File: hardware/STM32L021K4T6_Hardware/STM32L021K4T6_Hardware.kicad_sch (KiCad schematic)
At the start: 1 part, among them U1 STM32L021K4Tx

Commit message: schematic and footprints
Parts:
- added C1: 4u7, Capacitor_SMD:C_0805_2012Metric_Pad1.18x1.45mm_HandSolder, symbol Device:C_Small
- added C10: 10u, Capacitor_SMD:C_0805_2012Metric, symbol Device:C_Small
- added C2, C3, C6, C9: 100n, Capacitor_SMD:C_0805_2012Metric_Pad1.18x1.45mm_HandSolder, symbol Device:C_Small
- added C4: 1u, Capacitor_SMD:C_0805_2012Metric_Pad1.18x1.45mm_HandSolder, symbol Device:C_Small
- added C5: 10n, Capacitor_SMD:C_0805_2012Metric_Pad1.18x1.45mm_HandSolder, symbol Device:C_Small
- added C7, C8: 1uF, Capacitor_SMD:C_0805_2012Metric, symbol Device:C_Small
- added D1, D2: ~, LED_SMD:LED_0603_1608Metric_Pad1.05x0.95mm_HandSolder, symbol Device:LED_Small
- added J1: Conn_02x07_Odd_Even, Connector_PinHeader_1.27mm:PinHeader_2x07_P1.27mm_Vertical_SMD, symbol Connector_Generic:Conn_02x07_Odd_Even
- added J2: INPUT, Connector_JST:JST_XH_B2B-XH-A_1x02_P2.50mm_Vertical, symbol Connector_Generic:Conn_01x02
- added J3: POWER, Connector_JST:JST_XH_B2B-XH-A_1x02_P2.50mm_Vertical, symbol Connector_Generic:Conn_01x02
- added J4: OUTPUT, Connector_JST:JST_XH_B2B-XH-A_1x02_P2.50mm_Vertical, symbol Connector_Generic:Conn_01x02
- added L1: 39n, Inductor_SMD:L_0805_2012Metric_Pad1.05x1.20mm_HandSolder, symbol Device:L_Small
- added R1, R3: 1k, Resistor_SMD:R_0805_2012Metric_Pad1.20x1.40mm_HandSolder, symbol Device:R_Small
- added R2: 100k, Resistor_SMD:R_0805_2012Metric_Pad1.20x1.40mm_HandSolder, symbol Device:R_Small
- added U2: MCP1802x-xx02xOT, Package_TO_SOT_SMD:SOT-23-5, symbol Regulator_Linear:MCP1802x-xx02xOT
- added U3: MCP4801, Package_SO:SOIC-8_3.9x4.9mm_P1.27mm, symbol Analog_DAC:MCP4801
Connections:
- net +3.3V: now also C1.1, C2.1, C3.1, C8.1, D2.2 (A), J1.3 (Pin_3), L1.1, U2.5 (VOUT)
- net +3.3VA: now also C10.1, C4.1, C5.1, C9.1, L1.2, U3.1 (Vdd), U3.6 (~{SHDN})
- net GND: now also C1.2, C10.2, C2.2, C3.2, C4.2, C5.2, C6.2, C7.2, C8.2, C9.2, J1.11 (Pin_11), J1.5 (Pin_5), J1.7 (Pin_7), J2.2 (Pin_2), J3.2 (Pin_2), J4.2 (Pin_2), R1.2, R2.2, R3.2, U2.2 (GND), U3.7 (Vss)
- net DAC_nCS: now reaches U1.10 (PA4)
- net DAC_nCS: now also U3.2 (~{CS})
- net SPI1_SCK: now reaches U1.11 (PA5)
- net SPI1_SCK: now also U3.3 (SCK)
- net SPI1_MOSI: now reaches U1.13 (PA7)
- net SPI1_MOSI: now also U3.4 (SDI)
- net LED_STATUS: now reaches U1.18 (PA8)
- net LED_STATUS: now also D1.2 (A)
- net SWDIO: now reaches U1.23 (PA13)
- net SWDIO: now also J1.4 (Pin_4)
- net SWDCK: now reaches U1.24 (PA14)
- net SWDCK: now also J1.6 (Pin_6)
- net at U1.31 (PB9): now also R2.1
- net NRST: now reaches U1.4 (NRST)
- net NRST: now also C6.1, J1.12 (Pin_12)
- net USART2_RX: now reaches U1.6 (PA0)
- net USART2_RX: now also J1.13 (Pin_13)
- net ADC_IN1: now reaches U1.7 (PA1)
- net ADC_IN1: now also J2.1 (Pin_1)
- net USART2_TX: now reaches U1.8 (PA2)
- net USART2_TX: now also J1.14 (Pin_14)
- net DAC_nLDAC: now reaches U1.9 (PA3)
- net DAC_nLDAC: now also U3.5 (~{LDAC})
- new net: D1.1 (K), R1.1
- new net: D2.1 (K), R3.1
- new net +5V: C7.1, J3.1 (Pin_1), U2.1 (VIN), U2.3 (~{SHDN})
- new net DAC_OUT: J4.1 (Pin_1), U3.8 (Vout)
- no-connect marks 0 -> 20
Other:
- note added: "DAC MCP4801"
- note added: "IO Connectors"
- note added: "Power supply"
- note added: "STM32 Microcontroller"
- note added: "SWD Connector"

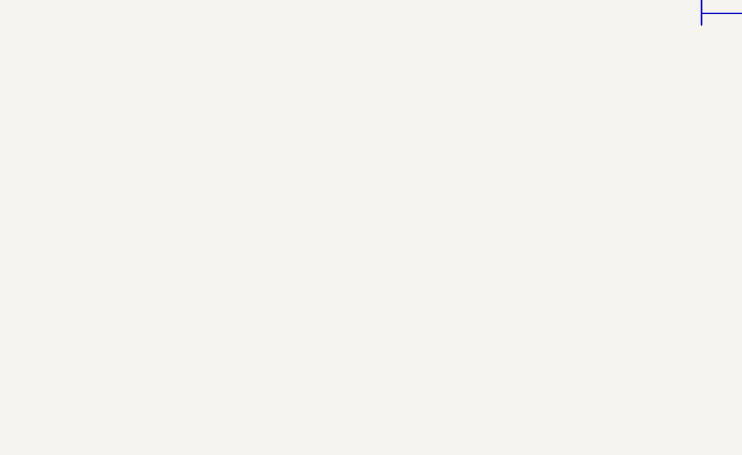
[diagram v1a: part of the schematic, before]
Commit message: add mounting holes
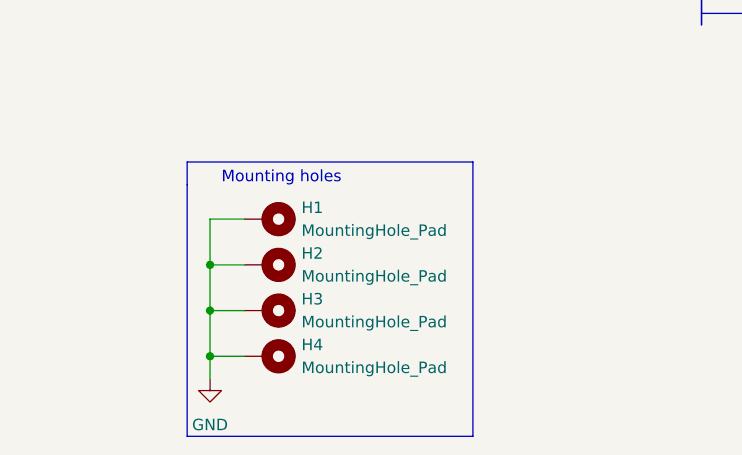
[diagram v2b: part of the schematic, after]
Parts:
- added H1, H2, H3, H4: MountingHole_Pad, MountingHole:MountingHole_3.2mm_M3_Pad, symbol Mechanical:MountingHole_Pad
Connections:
- net GND: now also H1.1, H2.1, H3.1, H4.1
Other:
- note added: "Mounting holes"
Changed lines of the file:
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@@
   (junction (at 27.94 44.45) (diameter 0) (color 0 0 0 0)
   )
+  (junction (at 40.64 157.48) (diameter 0) (color 0 0 0 0)
+  )
   (junction (at 146.05 39.37) (diameter 0) (color 0 0 0 0)
   )
@@
   (junction (at 111.76 38.1) (diameter 0) (color 0 0 0 0)
   )
+  (junction (at 40.64 147.32) (diameter 0) (color 0 0 0 0)
+  )
   (junction (at 69.85 77.47) (diameter 0) (color 0 0 0 0)
   )
@@
   )
   (junction (at 158.75 39.37) (diameter 0) (color 0 0 0 0)
+  )
+  (junction (at 40.64 152.4) (diameter 0) (color 0 0 0 0)
   )
   (junction (at 146.05 48.26) (diameter 0) (color 0 0 0 0)
@@
     (stroke (width 0) (type default))
   )
+  (wire (pts (xy 40.64 152.4) (xy 40.64 157.48))
+    (stroke (width 0) (type default))
+  )
   (wire (pts (xy 190.5 96.52) (xy 190.5 100.33))
     (stroke (width 0) (type default))
@@
     (stroke (width 0) (type default))
   )
+  (polyline (pts (xy 69.85 135.89) (xy 38.1 135.89))
+    (stroke (width 0) (type default))
+  )
   (wire (pts (xy 124.46 57.15) (xy 124.46 58.42))
     (stroke (width 0) (type default))
@@
     (stroke (width 0) (type default))
   )
+  (polyline (pts (xy 38.1 138.43) (xy 38.1 166.37))
+    (stroke (width 0) (type default))
+  )
   (wire (pts (xy 102.87 90.17) (xy 102.87 93.98))
     (stroke (width 0) (type default))
@@
     (stroke (width 0) (type default))
   )
+  (wire (pts (xy 44.45 152.4) (xy 40.64 152.4))
+    (stroke (width 0) (type default))
+  )
+  (wire (pts (xy 44.45 147.32) (xy 40.64 147.32))
+    (stroke (width 0) (type default))
+  )
   (wire (pts (xy 111.76 96.52) (xy 111.76 101.6))
     (stroke (width 0) (type default))
@@
     (stroke (width 0) (type default))
   )
+  (wire (pts (xy 40.64 157.48) (xy 40.64 160.02))
+    (stroke (width 0) (type default))
+  )
   (wire (pts (xy 195.58 82.55) (xy 198.12 82.55))
     (stroke (width 0) (type default))
@@
     (stroke (width 0) (type default))
   )
+  (wire (pts (xy 44.45 142.24) (xy 40.64 142.24))
+    (stroke (width 0) (type default))
+  )
   (wire (pts (xy 111.76 40.64) (xy 111.76 38.1))
     (stroke (width 0) (type default))
@@
     (stroke (width 0) (type default))
   )
+  (wire (pts (xy 44.45 157.48) (xy 40.64 157.48))
+    (stroke (width 0) (type default))
+  )
   (wire (pts (xy 212.09 96.52) (xy 212.09 100.33))
     (stroke (width 0) (type default))
@@
     (stroke (width 0) (type default))
   )
+  (wire (pts (xy 40.64 142.24) (xy 40.64 147.32))
+    (stroke (width 0) (type default))
+  )
   (wire (pts (xy 27.94 55.88) (xy 45.72 55.88))
     (stroke (width 0) (type default))
   )
+  (wire (pts (xy 40.64 147.32) (xy 40.64 152.4))
+    (stroke (width 0) (type default))
+  )
   (wire (pts (xy 27.94 44.45) (xy 34.29 44.45))
     (stroke (width 0) (type default))
@@
     (stroke (width 0) (type default))
   )
+  (polyline (pts (xy 38.1 135.89) (xy 38.1 138.43))
+    (stroke (width 0) (type default))
+  )
   (wire (pts (xy 102.87 99.06) (xy 102.87 101.6))
     (stroke (width 0) (type default))
@@
     (stroke (width 0) (type default))
   )
+  (polyline (pts (xy 69.85 166.37) (xy 69.85 135.89))
+    (stroke (width 0) (type default))
+  )
   (wire (pts (xy 158.75 45.72) (xy 158.75 48.26))
     (stroke (width 0) (type default))
@@
   )
   (wire (pts (xy 69.85 44.45) (xy 69.85 46.99))
+    (stroke (width 0) (type default))
+  )
+  (polyline (pts (xy 38.1 166.37) (xy 69.85 166.37))
     (stroke (width 0) (type default))
   )
@@
   )
   (text "DAC MCP4801\n" (at 24.13 71.12 0)
+    (effects (font (size 1.27 1.27)) (justify left bottom))
+  )
+  (text "Mounting holes" (at 41.91 138.43 0)
     (effects (font (size 1.27 1.27)) (justify left bottom))
   )
@@
         (path "/e06d2f29-0c33-4814-a609-8c0f42581a21"
           (reference "#PWR023") (unit 1)
+        )
+      )
+    )
+  )
+  (symbol (lib_id "Mechanical:MountingHole_Pad") (at 46.99 152.4 270) (unit 1)
+    (in_bom yes) (on_board yes) (dnp no) (fields_autoplaced)
+    (property "Reference" "H3" (at 50.8 151.13 90)
+      (effects (font (size 1.27 1.27)) (justify left))
+    )
+    (property "Value" "MountingHole_Pad" (at 50.8 153.67 90)
+      (effects (font (size 1.27 1.27)) (justify left))
+    )
+    (property "Footprint" "MountingHole:MountingHole_3.2mm_M3_Pad" (at 46.99 152.4 0)
+      (effects (font (size 1.27 1.27)) hide)
+    )
+    (property "Datasheet" "~" (at 46.99 152.4 0)
+      (effects (font (size 1.27 1.27)) hide)
+    )
+    (pin "1")
+    (instances
+      (project "STM32L021K4T6_Hardware"
+        (path "/e06d2f29-0c33-4814-a609-8c0f42581a21"
+          (reference "H3") (unit 1)
+        )
+      )
+    )
+  )
+  (symbol (lib_id "Mechanical:MountingHole_Pad") (at 46.99 157.48 270) (unit 1)
+    (in_bom yes) (on_board yes) (dnp no) (fields_autoplaced)
+    (property "Reference" "H4" (at 50.8 156.21 90)
+      (effects (font (size 1.27 1.27)) (justify left))
+    )
+    (property "Value" "MountingHole_Pad" (at 50.8 158.75 90)
+      (effects (font (size 1.27 1.27)) (justify left))
+    )
+    (property "Footprint" "MountingHole:MountingHole_3.2mm_M3_Pad" (at 46.99 157.48 0)
+      (effects (font (size 1.27 1.27)) hide)
+    )
+    (property "Datasheet" "~" (at 46.99 157.48 0)
+      (effects (font (size 1.27 1.27)) hide)
+    )
+    (pin "1")
+    (instances
+      (project "STM32L021K4T6_Hardware"
+        (path "/e06d2f29-0c33-4814-a609-8c0f42581a21"
+          (reference "H4") (unit 1)
+        )
+      )
+    )
+  )
+  (symbol (lib_id "Mechanical:MountingHole_Pad") (at 46.99 142.24 270) (unit 1)
+    (in_bom yes) (on_board yes) (dnp no) (fields_autoplaced)
+    (property "Reference" "H1" (at 50.8 140.97 90)
+      (effects (font (size 1.27 1.27)) (justify left))
+    )
+    (property "Value" "MountingHole_Pad" (at 50.8 143.51 90)
+      (effects (font (size 1.27 1.27)) (justify left))
+    )
+    (property "Footprint" "MountingHole:MountingHole_3.2mm_M3_Pad" (at 46.99 142.24 0)
+      (effects (font (size 1.27 1.27)) hide)
+    )
+    (property "Datasheet" "~" (at 46.99 142.24 0)
+      (effects (font (size 1.27 1.27)) hide)
+    )
+    (pin "1")
+    (instances
+      (project "STM32L021K4T6_Hardware"
+        (path "/e06d2f29-0c33-4814-a609-8c0f42581a21"
+          (reference "H1") (unit 1)
         )
       )
@@
         )
       )
+    )
+  )
+  (symbol (lib_id "Mechanical:MountingHole_Pad") (at 46.99 147.32 270) (unit 1)
+    (in_bom yes) (on_board yes) (dnp no) (fields_autoplaced)
+    (property "Reference" "H2" (at 50.8 146.05 90)
+      (effects (font (size 1.27 1.27)) (justify left))
+    )
+    (property "Value" "MountingHole_Pad" (at 50.8 148.59 90)
+      (effects (font (size 1.27 1.27)) (justify left))
+    )
+    (property "Footprint" "MountingHole:MountingHole_3.2mm_M3_Pad" (at 46.99 147.32 0)
+      (effects (font (size 1.27 1.27)) hide)
+    )
+    (property "Datasheet" "~" (at 46.99 147.32 0)
+      (effects (font (size 1.27 1.27)) hide)
+    )
+    (pin "1")
+    (instances
+      (project "STM32L021K4T6_Hardware"
+        (path "/e06d2f29-0c33-4814-a609-8c0f42581a21"
+          (reference "H2") (unit 1)
+        )
+      )
+    )
+  )
+  (symbol (lib_id "power:GND") (at 40.64 160.02 0) (unit 1)
+    (in_bom yes) (on_board yes) (dnp no) (fields_autoplaced)
+    (property "Reference" "#PWR026" (at 40.64 166.37 0)
+      (effects (font (size 1.27 1.27)) hide)
+    )
+    (property "Value" "GND" (at 40.64 165.1 0)
+      (effects (font (size 1.27 1.27)))
+    )
+    (property "Footprint" "" (at 40.64 160.02 0)
+      (effects (font (size 1.27 1.27)) hide)
+    )
+    (property "Datasheet" "" (at 40.64 160.02 0)
+      (effects (font (size 1.27 1.27)) hide)
+    )
+    (pin "1")
+    (instances
+      (project "STM32L021K4T6_Hardware"
+        (path "/e06d2f29-0c33-4814-a609-8c0f42581a21"
+          (reference "#PWR026") (unit 1)
+        )
+      )
